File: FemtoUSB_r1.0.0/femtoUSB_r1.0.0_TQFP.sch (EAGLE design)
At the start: 27 parts, among them IC1 ATSAMD21E18A-AU

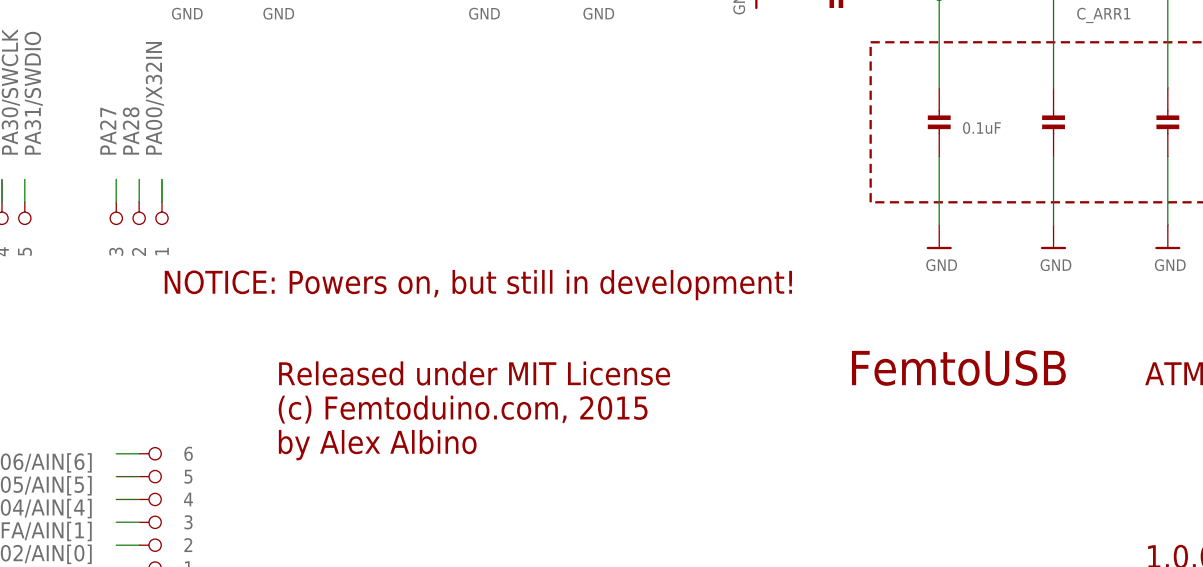
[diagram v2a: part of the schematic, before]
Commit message: Adding in PDFs, removing Notice labels, as boards appear to work now
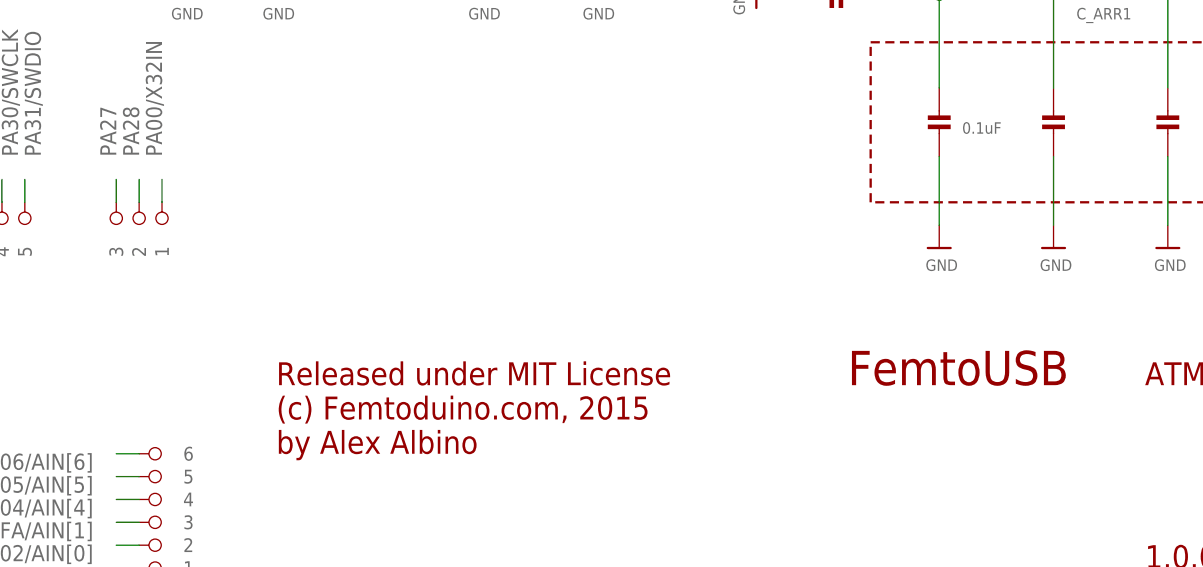
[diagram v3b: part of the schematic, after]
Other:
- note removed: "NOTICE: Powers on, but still in development!"
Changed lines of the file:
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@@
 <grid distance="0.1" unitdist="inch" unit="inch" style="lines" multiple="1" display="no" altdistance="0.01" altunitdist="inch" altunit="inch"/>
 <layers>
-<layer number="1" name="Top" color="4" fill="1" visible="yes" active="no"/>
-<layer number="2" name="Route2" color="1" fill="3" visible="yes" active="no"/>
-<layer number="3" name="Route3" color="4" fill="3" visible="yes" active="no"/>
-<layer number="14" name="Route14" color="1" fill="6" visible="yes" active="no"/>
-<layer number="15" name="Route15" color="4" fill="6" visible="yes" active="no"/>
-<layer number="16" name="Bottom" color="1" fill="1" visible="yes" active="no"/>
-<layer number="17" name="Pads" color="2" fill="1" visible="yes" active="no"/>
-<layer number="18" name="Vias" color="2" fill="1" visible="yes" active="no"/>
-<layer number="19" name="Unrouted" color="6" fill="1" visible="yes" active="no"/>
-<layer number="20" name="Dimension" color="15" fill="1" visible="yes" active="no"/>
-<layer number="21" name="tPlace" color="7" fill="1" visible="yes" active="no"/>
-<layer number="22" name="bPlace" color="7" fill="1" visible="yes" active="no"/>
-<layer number="23" name="tOrigins" color="15" fill="1" visible="yes" active="no"/>
-<layer number="24" name="bOrigins" color="15" fill="1" visible="yes" active="no"/>
-<layer number="25" name="tNames" color="7" fill="1" visible="yes" active="no"/>
-<layer number="26" name="bNames" color="7" fill="1" visible="yes" active="no"/>
-<layer number="27" name="tValues" color="7" fill="1" visible="yes" active="no"/>
-<layer number="28" name="bValues" color="7" fill="1" visible="yes" active="no"/>
+<layer number="1" name="Top" color="4" fill="1" visible="no" active="no"/>
+<layer number="2" name="Route2" color="1" fill="3" visible="no" active="no"/>
+<layer number="3" name="Route3" color="4" fill="3" visible="no" active="no"/>
+<layer number="14" name="Route14" color="1" fill="6" visible="no" active="no"/>
+<layer number="15" name="Route15" color="4" fill="6" visible="no" active="no"/>
+<layer number="16" name="Bottom" color="1" fill="1" visible="no" active="no"/>
+<layer number="17" name="Pads" color="2" fill="1" visible="no" active="no"/>
+<layer number="18" name="Vias" color="2" fill="1" visible="no" active="no"/>
+<layer number="19" name="Unrouted" color="6" fill="1" visible="no" active="no"/>
+<layer number="20" name="Dimension" color="15" fill="1" visible="no" active="no"/>
+<layer number="21" name="tPlace" color="7" fill="1" visible="no" active="no"/>
+<layer number="22" name="bPlace" color="7" fill="1" visible="no" active="no"/>
+<layer number="23" name="tOrigins" color="15" fill="1" visible="no" active="no"/>
+<layer number="24" name="bOrigins" color="15" fill="1" visible="no" active="no"/>
+<layer number="25" name="tNames" color="7" fill="1" visible="no" active="no"/>
+<layer number="26" name="bNames" color="7" fill="1" visible="no" active="no"/>
+<layer number="27" name="tValues" color="7" fill="1" visible="no" active="no"/>
+<layer number="28" name="bValues" color="7" fill="1" visible="no" active="no"/>
 <layer number="29" name="tStop" color="7" fill="3" visible="no" active="no"/>
 <layer number="30" name="bStop" color="7" fill="6" visible="no" active="no"/>
@@
 <layer number="35" name="tGlue" color="7" fill="4" visible="no" active="no"/>
 <layer number="36" name="bGlue" color="7" fill="5" visible="no" active="no"/>
-<layer number="37" name="tTest" color="7" fill="1" visible="yes" active="no"/>
-<layer number="38" name="bTest" color="7" fill="1" visible="yes" active="no"/>
+<layer number="37" name="tTest" color="7" fill="1" visible="no" active="no"/>
+<layer number="38" name="bTest" color="7" fill="1" visible="no" active="no"/>
 <layer number="39" name="tKeepout" color="4" fill="11" visible="no" active="no"/>
 <layer number="40" name="bKeepout" color="1" fill="11" visible="no" active="no"/>
@@
 <layer number="44" name="Drills" color="7" fill="1" visible="no" active="no"/>
 <layer number="45" name="Holes" color="7" fill="1" visible="no" active="no"/>
-<layer number="46" name="Milling" color="3" fill="1" visible="yes" active="no"/>
-<layer number="47" name="Measures" color="7" fill="1" visible="yes" active="no"/>
-<layer number="48" name="Document" color="7" fill="1" visible="yes" active="no"/>
-<layer number="49" name="Reference" color="7" fill="1" visible="yes" active="no"/>
-<layer number="50" name="dxf" color="7" fill="1" visible="yes" active="no"/>
-<layer number="51" name="tDocu" color="7" fill="1" visible="yes" active="no"/>
-<layer number="52" name="bDocu" color="7" fill="1" visible="yes" active="no"/>
-<layer number="53" name="tGND_GNDA" color="7" fill="9" visible="yes" active="no"/>
-<layer number="54" name="bGND_GNDA" color="1" fill="9" visible="yes" active="no"/>
-<layer number="56" name="wert" color="7" fill="1" visible="yes" active="no"/>
+<layer number="46" name="Milling" color="3" fill="1" visible="no" active="no"/>
+<layer number="47" name="Measures" color="7" fill="1" visible="no" active="no"/>
+<layer number="48" name="Document" color="7" fill="1" visible="no" active="no"/>
+<layer number="49" name="Reference" color="7" fill="1" visible="no" active="no"/>
+<layer number="50" name="dxf" color="7" fill="1" visible="no" active="no"/>
+<layer number="51" name="tDocu" color="7" fill="1" visible="no" active="no"/>
+<layer number="52" name="bDocu" color="7" fill="1" visible="no" active="no"/>
+<layer number="53" name="tGND_GNDA" color="7" fill="9" visible="no" active="no"/>
+<layer number="54" name="bGND_GNDA" color="1" fill="9" visible="no" active="no"/>
+<layer number="56" name="wert" color="7" fill="1" visible="no" active="no"/>
 <layer number="91" name="Nets" color="2" fill="1" visible="yes" active="yes"/>
 <layer number="92" name="Busses" color="1" fill="1" visible="yes" active="yes"/>
@@
 (c) Femtoduino.com, 2015
 by Alex Albino</text>
-<text x="73.66" y="38.1" size="2.54" layer="94" font="vector">NOTICE: Powers on, but still in development!</text>
 </plain>
 <instances>

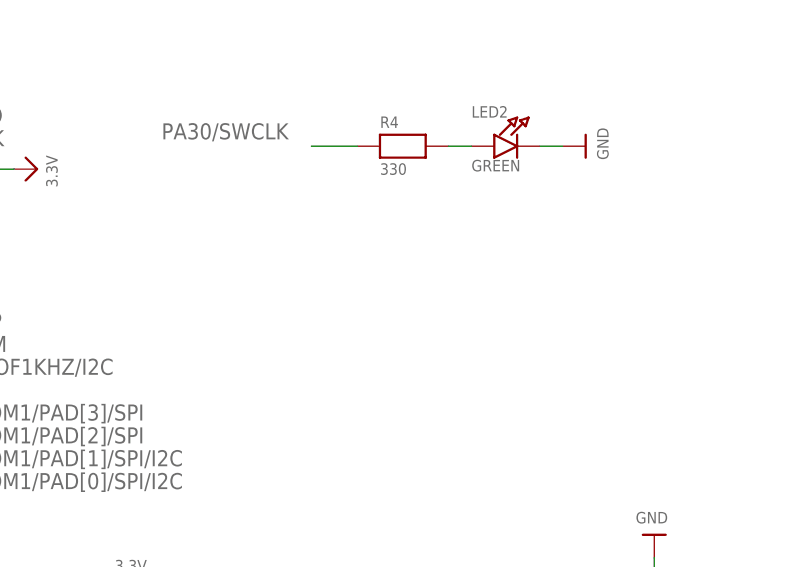
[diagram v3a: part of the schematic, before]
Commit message: Updating r1.x version of FemtoUSB (QFN and QFP chip version). Pin PA15 and GND pads now available to start board up in bootloader mode (SAM-BA)
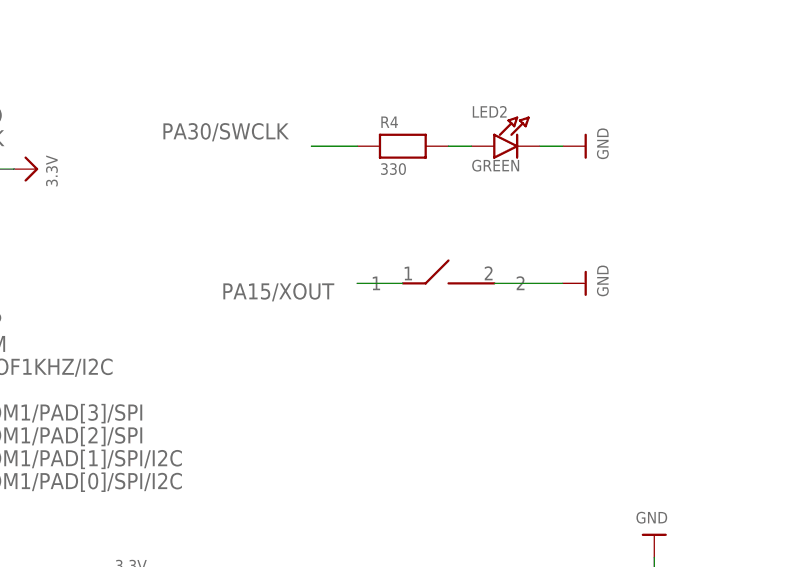
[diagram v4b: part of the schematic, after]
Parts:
- added U$38: SPST_SMD, femtoduino:SPST_SMD
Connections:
- net GND: now also U$38.2
- net PA15/XOUT: now also U$38.1
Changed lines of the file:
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@@
 <part name="U$36" library="microbuilder" deviceset="3.3V" device=""/>
 <part name="U$37" library="microbuilder" deviceset="3.3V" device=""/>
+<part name="U$38" library="femtoduino" deviceset="SPST_SMD" device=""/>
+<part name="U$39" library="microbuilder" deviceset="GND" device=""/>
 </parts>
 <sheets>
@@
 <instance part="U$36" gate="G$1" x="185.42" y="83.82"/>
 <instance part="U$37" gate="G$1" x="111.76" y="162.56" rot="R270"/>
+<instance part="U$38" gate="G$1" x="160.02" y="149.86"/>
+<instance part="U$39" gate="G$1" x="172.72" y="149.86" rot="R90"/>
 </instances>
 <busses>
@@
 <label x="236.22" y="114.3" size="1.778" layer="95"/>
 </segment>
+<segment>
+<pinref part="U$38" gate="G$1" pin="1"/>
+<wire x1="152.4" y1="149.86" x2="147.32" y2="149.86" width="0.1524" layer="91"/>
+<label x="144.78" y="149.86" size="1.778" layer="95" rot="R180"/>
+</segment>
 </net>
 <net name="PA16/SERCOM1/PAD[0]/SPI/I2C" class="0">
@@
 <pinref part="C8" gate="G$1" pin="P$1"/>
 </segment>
-</net>
+<segment>
+<pinref part="U$38" gate="G$1" pin="2"/>
+<wire x1="162.56" y1="149.86" x2="170.18" y2="149.86" width="0.1524" layer="91"/>
+<pinref part="U$39" gate="G$1" pin="GND"/>
+</segment>
+</net>

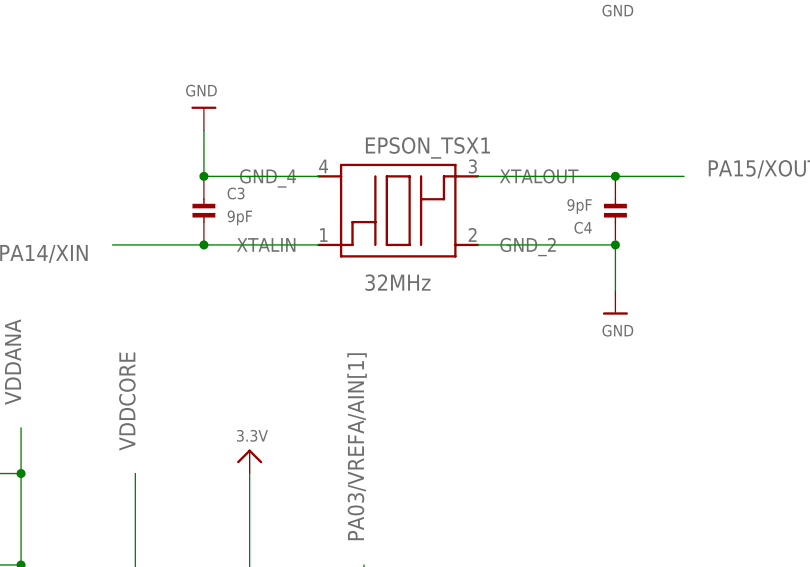
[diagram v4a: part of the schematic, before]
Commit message: Updating gerbers and BoM/Partslist of QFN version
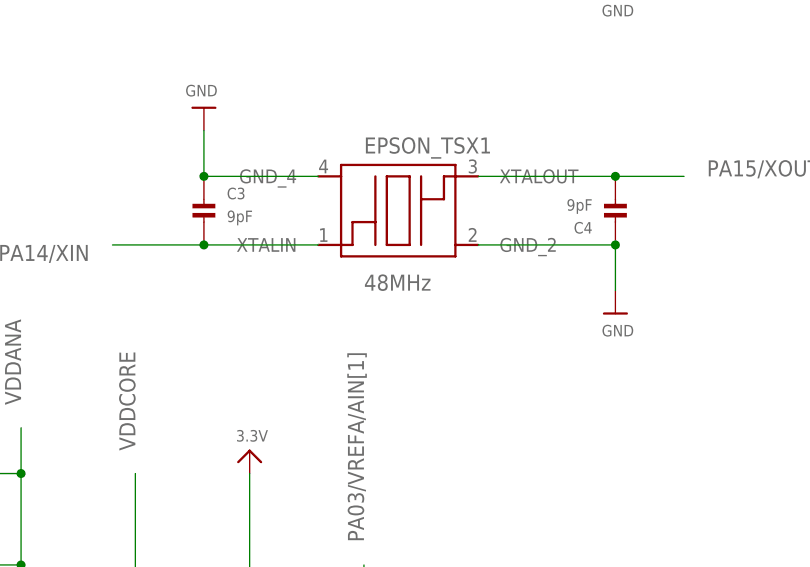
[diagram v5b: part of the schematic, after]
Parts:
- EPSON_TSX1: value 32MHz -> 48MHz
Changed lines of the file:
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@@
 <part name="U$24" library="microbuilder" deviceset="GND" device=""/>
 <part name="U$25" library="microbuilder" deviceset="GND" device=""/>
-<part name="EPSON_TSX1" library="crystals" deviceset="TSX-3225" device="" value="32MHz">
+<part name="EPSON_TSX1" library="crystals" deviceset="TSX-3225" device="" value="48MHz">
 <attribute name="DIGIKEY_PART" value="TSX-3225 32.0000MF15X-B-ND"/>
 </part>
